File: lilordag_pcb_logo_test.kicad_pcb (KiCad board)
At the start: 2 copper layers, 98.1 x 100 mm, 178 parts, among them J1 USB4105-GF-A, J2 826629-7, J3 826629-7, Q1 BC846, Q2 BC846, Q3 MMBT3906, Q4 MMBT3906, Q5 BC846, Q6 BC846, Q7 SSM3J56MFV, Q8 SSM3J56MFV, SW1 PCM12SMTR, SW2 PCM12SMTR, U1 ESP32-C3-MINI-1-N4, U2 WS2812B-B, U3 WS2812B-B, U4 WS2812B-B, U5 WS2812B-B

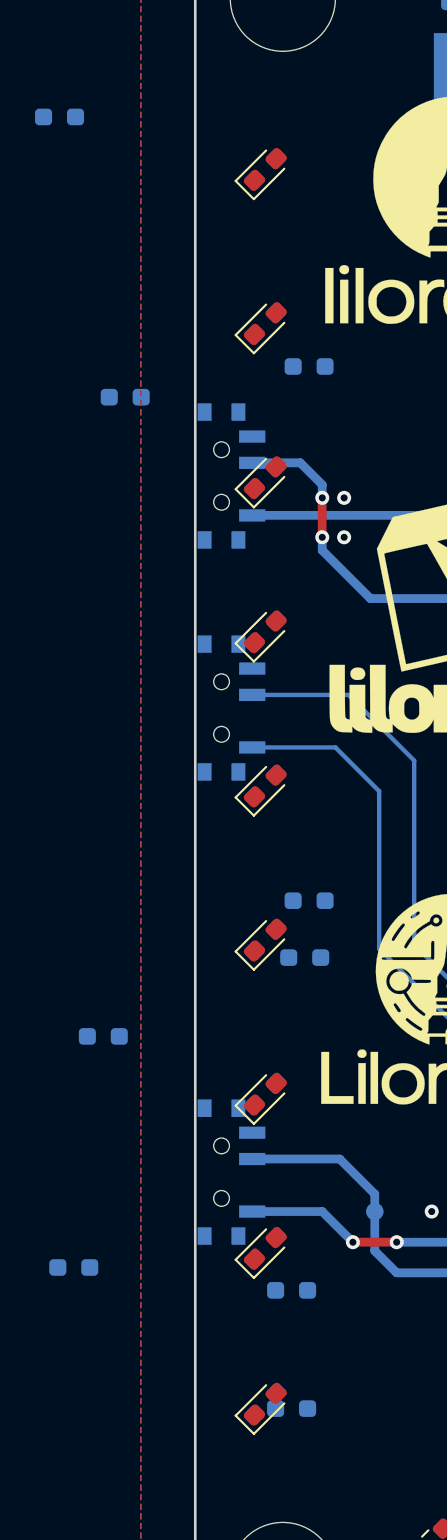
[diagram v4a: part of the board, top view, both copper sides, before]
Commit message: Left side LEDs arranged
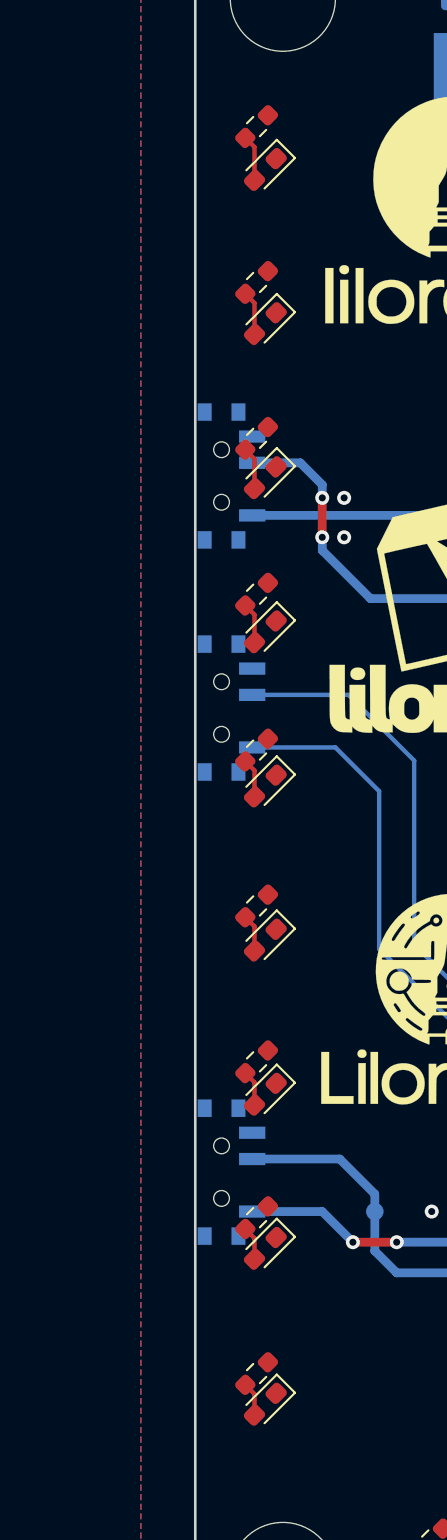
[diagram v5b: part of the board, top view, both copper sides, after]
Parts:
- R1, R25, R26, R27, R28, R4, R5, R6, R7: moved to F.Cu
- moved R27 17.8 mm to (31.5, 69.0), turned to -135 degrees
- moved R4 15.7 mm to (31.5, 95.7), turned to -135 degrees
- moved R5 12.2 mm to (31.5, 77.9), turned to -135 degrees
- moved R26 11.5 mm to (31.5, 86.8), turned to -135 degrees
- moved R7 11.3 mm to (31.5, 42.3), turned to -135 degrees
- moved R6 7.86 mm to (31.5, 60.1), turned to -135 degrees
- moved R28 5.66 mm to (31.5, 51.2), turned to -135 degrees
- moved R25 4.61 mm to (31.5, 104.6), turned to -135 degrees
- moved R1 2.83 mm to (31.5, 113.5), turned to -135 degrees
- turned D1 to -135 degrees
- turned D2 to -135 degrees
- turned D21 to -135 degrees
- turned D22 to -135 degrees
- turned D23 to -135 degrees
- turned D24 to -135 degrees
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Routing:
- net Net-(D5-Pad2): track 0.00 -> 2.64 mm
- net Net-(D24-Pad2): track 0.00 -> 2.54 mm
- net Net-(D4-Pad2): track 0.00 -> 2.44 mm
- net Net-(D23-Pad2): track 0.00 -> 2.34 mm
- net Net-(D3-Pad2): track 0.00 -> 2.24 mm
- net Net-(D22-Pad2): track 0.00 -> 2.14 mm
- net Net-(D2-Pad2): track 0.00 -> 2.04 mm
- net Net-(D1-Pad2): track 0.00 -> 1.94 mm
- net Net-(D21-Pad2): track 0.00 -> 1.94 mm

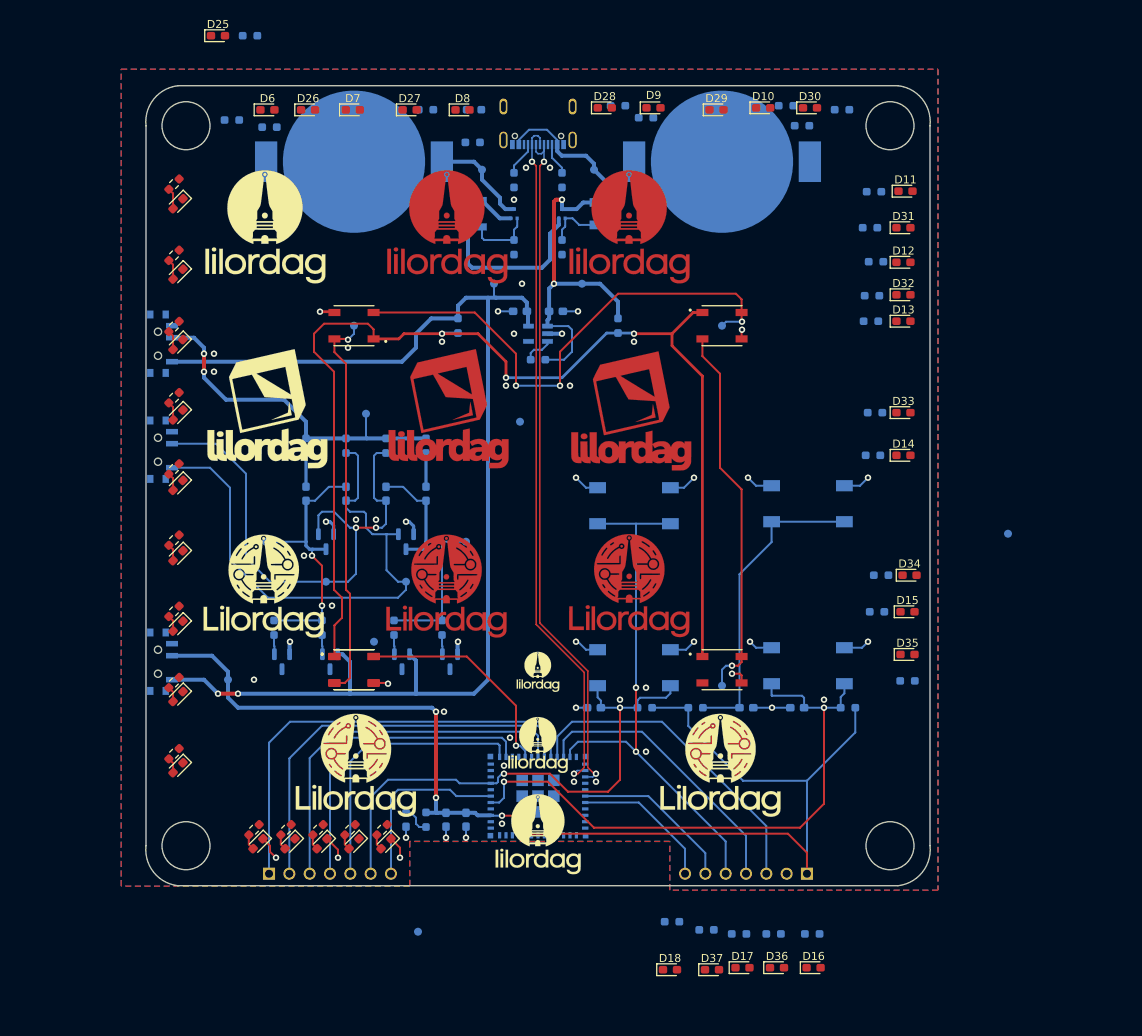
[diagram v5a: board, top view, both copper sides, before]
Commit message: Top LEDs arranged.
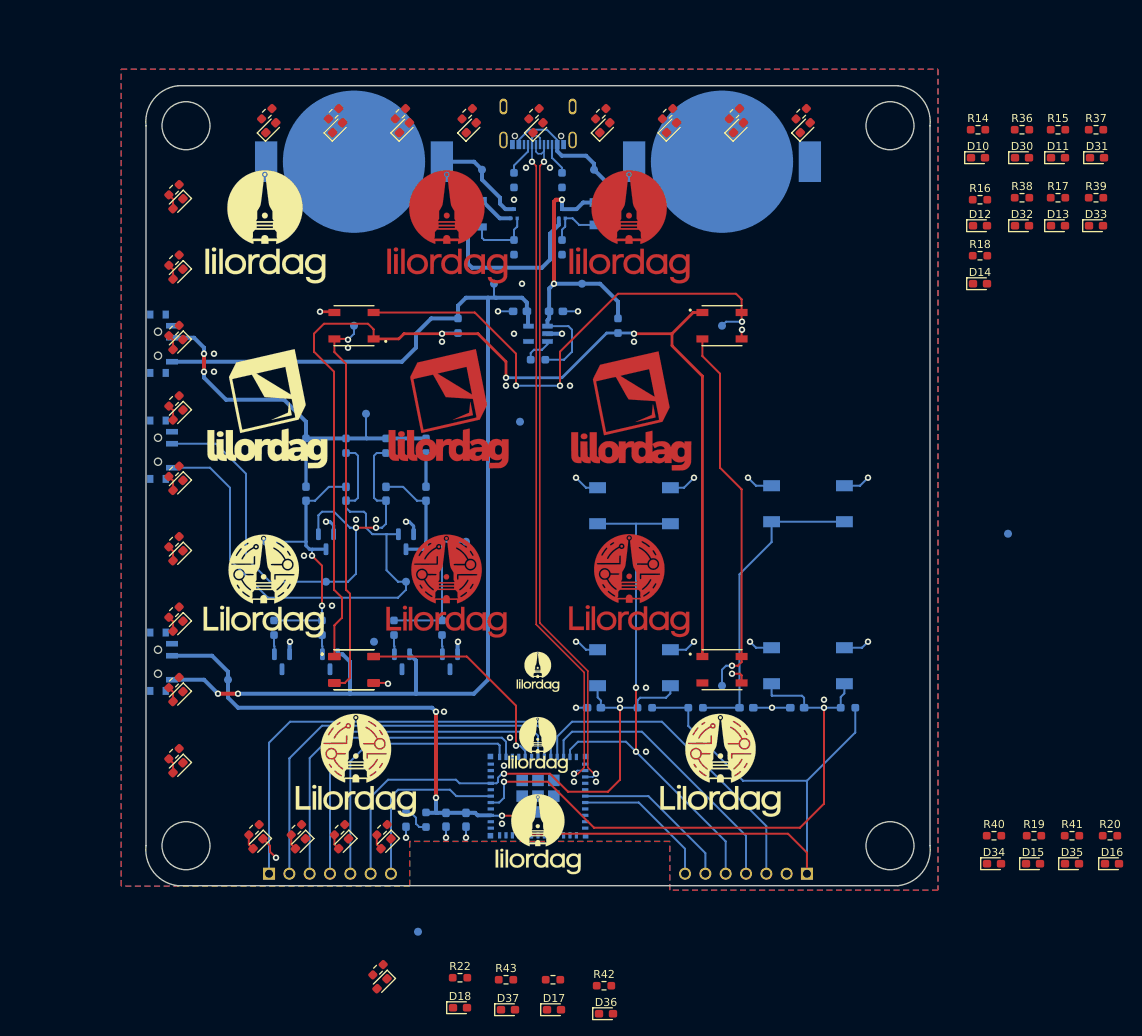
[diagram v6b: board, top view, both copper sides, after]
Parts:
- R11, R13, R14, R15, R16, R17, R18, R19, R20, R21, R22, R29, R30, R32, R34, R35, R36, R37, R38, R39, R40, R41, R42, R43, R8, R9: moved to F.Cu
- moved D16 39.5 mm to (148.8, 127.2)
- moved R20 39.2 mm to (148.5, 123.8), turned to 0 degrees
- moved R39 38.5 mm to (146.8, 44.0), turned to 0 degrees
- moved D34 37.6 mm to (134.0, 127.2)
- moved R40 35.5 mm to (134.0, 123.8), turned to 0 degrees
- moved D15 35.2 mm to (138.9, 127.2)
- moved R19 34.2 mm to (139.0, 123.8), turned to 0 degrees
- moved D33 33.5 mm to (146.8, 47.5)
- moved D35 33.3 mm to (143.8, 127.2)
- moved R37 30.8 mm to (146.8, 35.5), turned to 0 degrees
- moved R18 28.3 mm to (132.2, 51.2), turned to 0 degrees
- moved R41 28.2 mm to (143.8, 123.8), turned to 0 degrees
- moved R17 28.0 mm to (142.0, 44.0), turned to 0 degrees
- moved D10 27.6 mm to (132.0, 39.0)
- moved R22 27.4 mm to (67.2, 141.5), turned to 0 degrees
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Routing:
- net GND: track 65.5 -> 59.7 mm, vias 54 -> 51
- net Net-(D38-Pad2): track 1.94 -> 0.00 mm
- net Net-(D5-Pad2): track 2.64 -> 1.94 mm
- net Net-(D24-Pad2): track 2.54 -> 1.94 mm
- net Net-(D4-Pad2): track 2.44 -> 1.94 mm

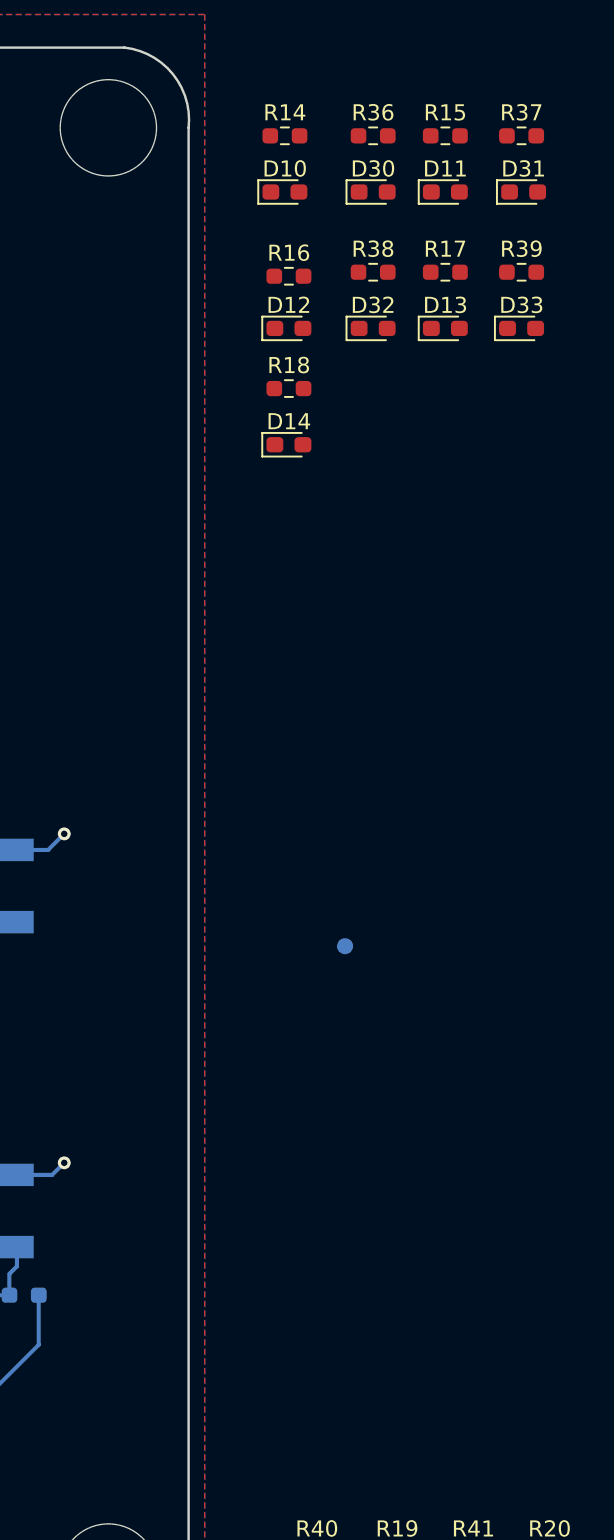
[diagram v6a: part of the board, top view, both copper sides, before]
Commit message: Right LEDs arranged
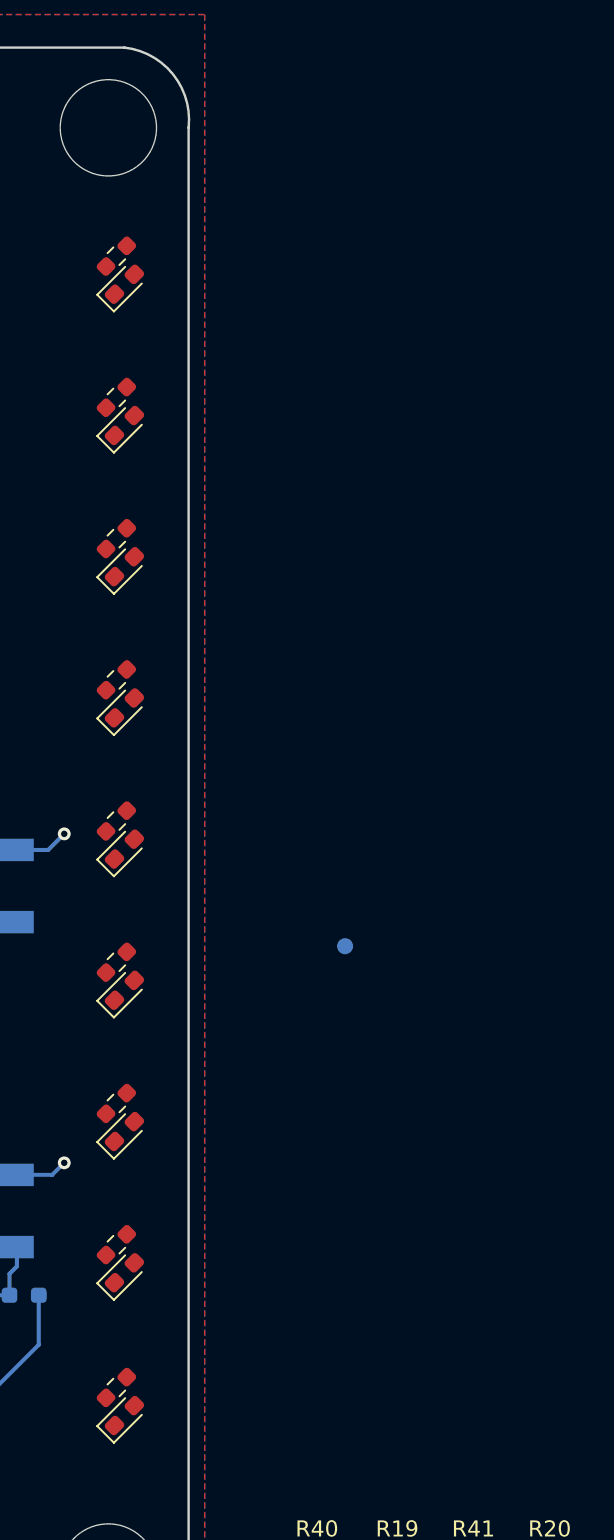
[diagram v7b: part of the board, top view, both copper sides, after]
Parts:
- moved R39 65.6 mm to (121.5, 104.6), turned to 45 degrees
- moved D33 63.8 mm to (122.0, 106.3), turned to 45 degrees
- moved R18 63.2 mm to (121.5, 113.5), turned to 45 degrees
- moved D14 61.4 mm to (122.0, 115.2), turned to 45 degrees
- moved R17 55.7 mm to (121.5, 95.8), turned to 45 degrees
- moved D13 53.9 mm to (122.0, 97.5), turned to 45 degrees
- moved R38 45.9 mm to (121.5, 87.0), turned to 45 degrees
- moved D32 44.1 mm to (122.0, 88.8), turned to 45 degrees
- moved R37 42.3 mm to (121.5, 69.4), turned to 45 degrees
- moved D31 40.6 mm to (122.0, 71.2), turned to 45 degrees
- moved R16 35.6 mm to (121.5, 78.2), turned to 45 degrees
- moved D12 34.0 mm to (122.0, 80.0), turned to 45 degrees
- moved R15 32.4 mm to (121.5, 60.6), turned to 45 degrees
- moved D11 30.7 mm to (122.0, 62.4), turned to 45 degrees
- moved R36 22.8 mm to (121.5, 51.8), turned to 45 degrees
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
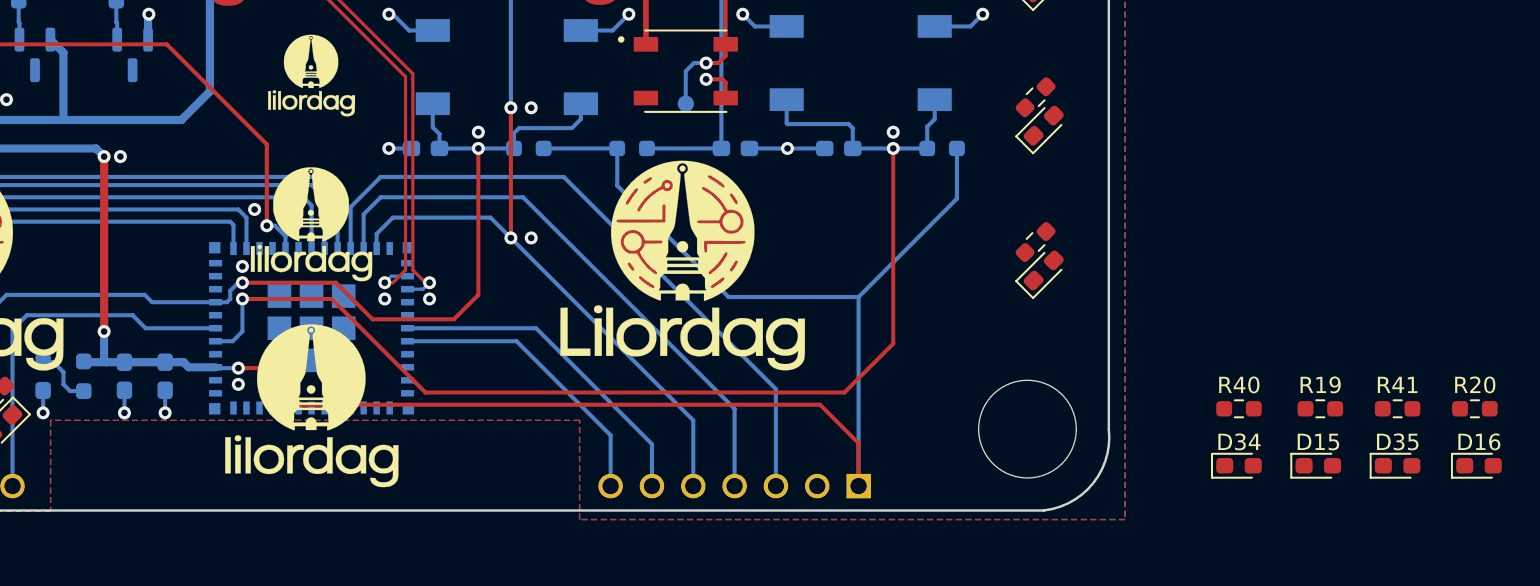
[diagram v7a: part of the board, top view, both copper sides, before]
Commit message: Bottom right LEDs arranged
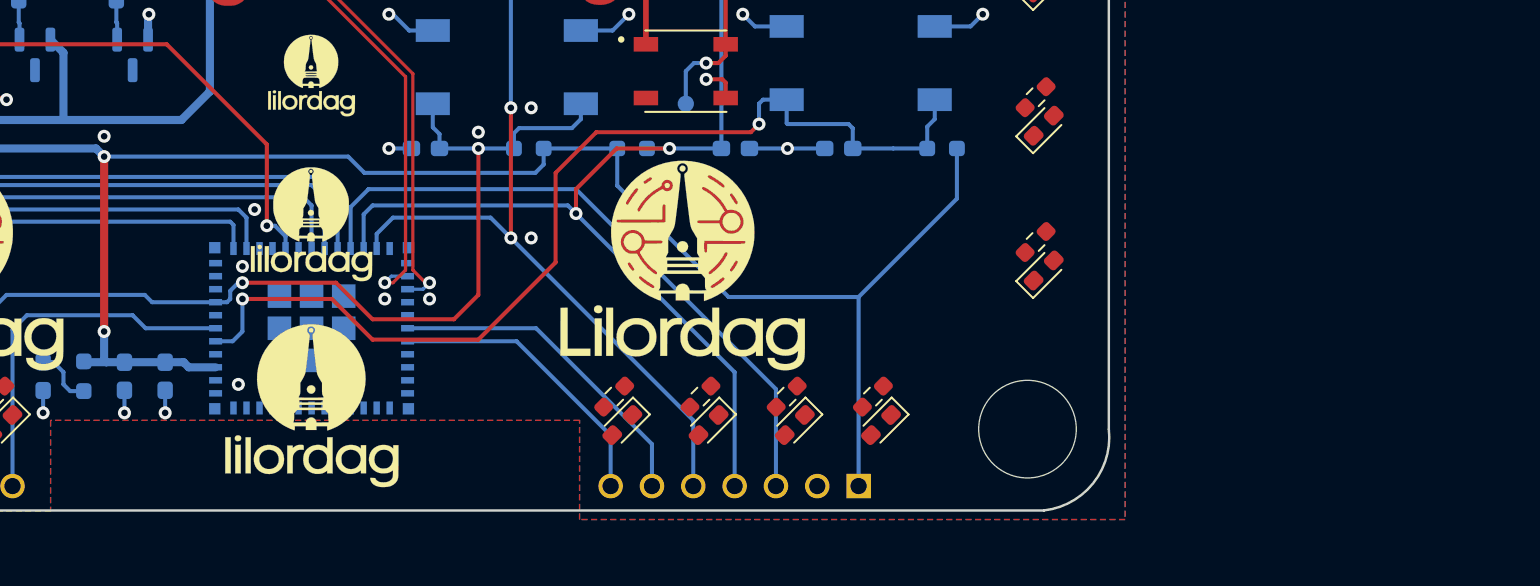
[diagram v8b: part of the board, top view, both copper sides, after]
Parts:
- moved R20 52.9 mm to (95.6, 123.0), turned to -135 degrees
- moved D16 52.7 mm to (96.1, 124.8), turned to -135 degrees
- moved R41 42.9 mm to (100.9, 123.0), turned to -135 degrees
- moved D35 42.4 mm to (101.4, 124.8), turned to -135 degrees
- moved R19 32.8 mm to (106.2, 123.0), turned to -135 degrees
- moved D15 32.3 mm to (106.7, 124.8), turned to -135 degrees
- moved R40 22.5 mm to (111.5, 123.0), turned to -135 degrees
- moved D34 22.1 mm to (112.0, 124.8), turned to -135 degrees
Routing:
- net V3.3-ESP: track 150.6 -> 135.2 mm, vias 3 -> 2
- net STRAP_IO2: track 74.2 -> 63.1 mm
- net STRAP_IO8: track 74.1 -> 83.2 mm, vias 0 -> 2
- net IO7: track 40.8 -> 40.2 mm
- net GND: vias 51 -> 50
